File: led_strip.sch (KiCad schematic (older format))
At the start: 4 parts

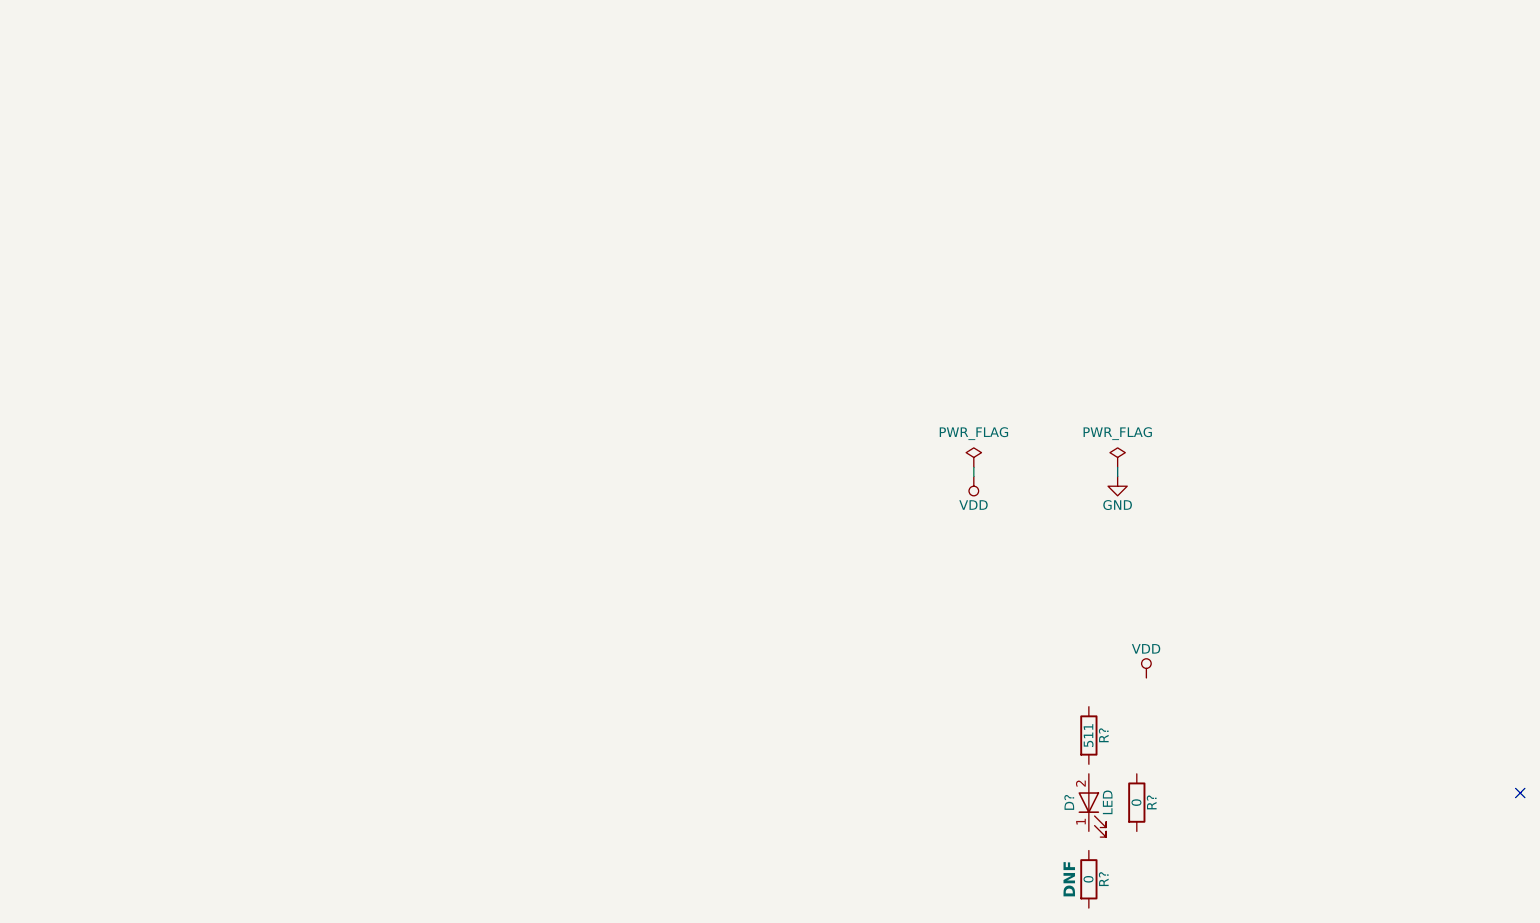
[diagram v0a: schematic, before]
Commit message: First two pages created for a hierarchical schematic. Using this as a test run to scale for the entire design
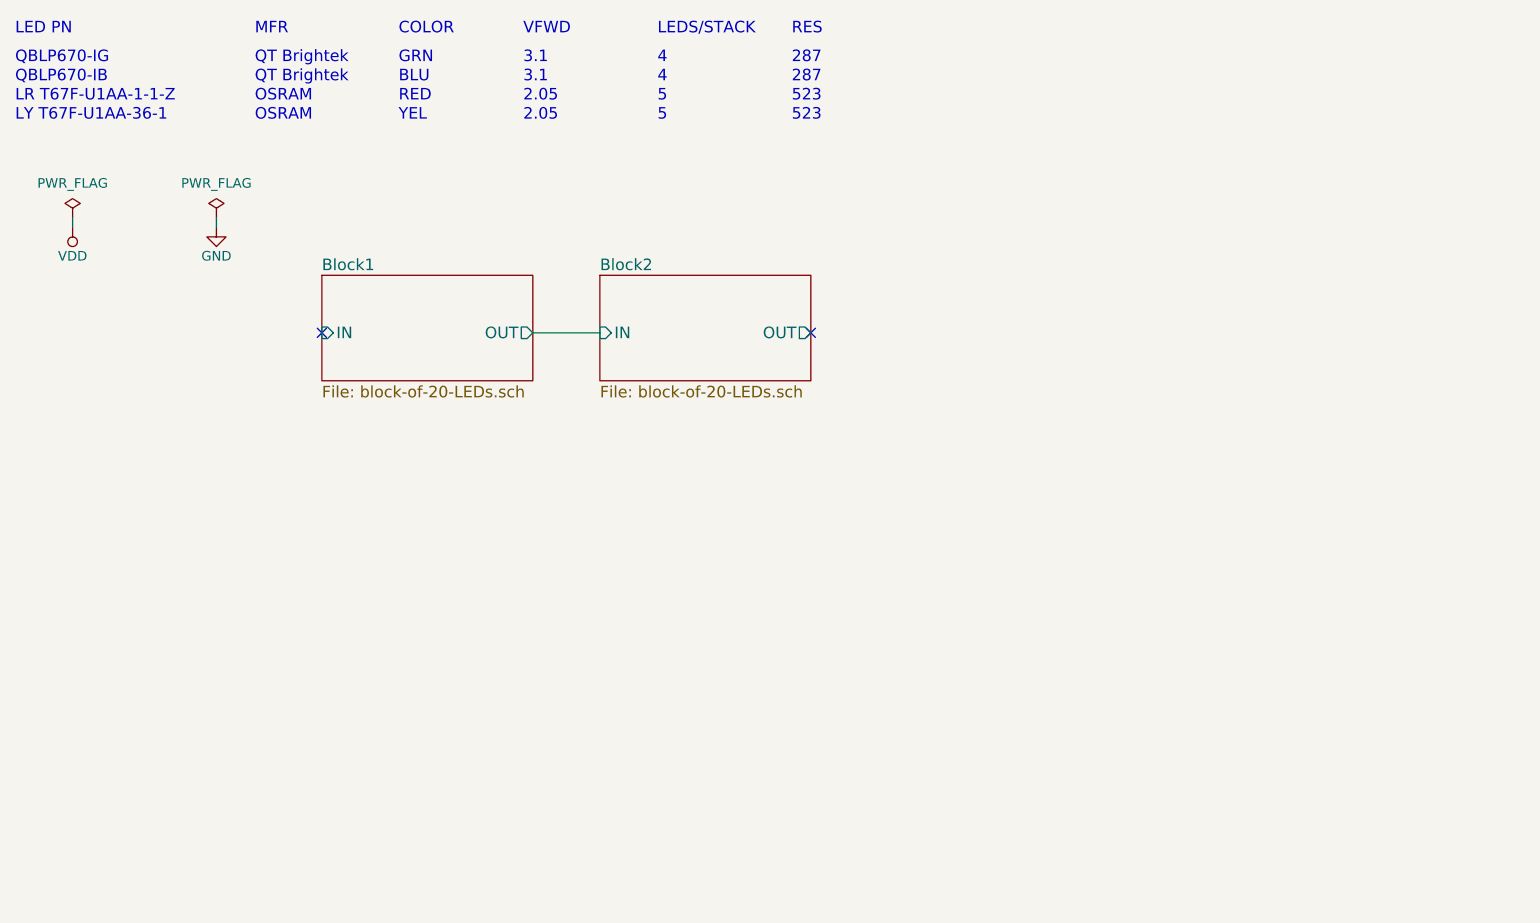
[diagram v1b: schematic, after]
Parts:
- removed D?: LED, symbol LED
- removed R?: 511, symbol R
- removed R? (x2): 0, symbol R
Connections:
- no-connect marks 1 -> 2
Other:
- note added: "2.05"
- note added: "287"
- note added: "3.1"
- note added: "4"
- note added: "5"
- note added: "523"
- note added: "BLU"
- note added: "COLOR"
- note added: "GRN"
- note added: "LED PN"
- note added: "LEDS/STACK"
- note added: "LR T67F-U1AA-1-1-Z"
- note added: "LY T67F-U1AA-36-1"
- note added: "MFR"
- note added: "OSRAM"
- note added: "QBLP670-IB"
- note added: "QBLP670-IG"
- note added: "QT Brightek"
- note added: "RED"
- note added: "RES"
- note added: "VFWD"
- note added: "YEL"
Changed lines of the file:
@@
 $Descr B 17000 11000
 encoding utf-8
-Sheet 1 1
+Sheet 1 3
 Title "LED Blade"
 Date ""
@@
 Comment4 ""
 $EndDescr
-Wire Wire Line
-	6550 3150 6550 3200
-Wire Wire Line
-	5800 3150 5800 3200
 $Comp
-L PWR_FLAG #FLG06
+L PWR_FLAG #FLG01
 U 1 1 59A4D1E2
-P 6550 3150
-F 0 "#FLG06" H 6550 3245 50  0001 C CNN
-F 1 "PWR_FLAG" H 6550 3330 50  0000 C CNN
-F 2 "" H 6550 3150 50  0000 C CNN
-F 3 "" H 6550 3150 50  0000 C CNN
-	1    6550 3150
+P 1850 1850
+F 0 "#FLG01" H 1850 1945 50  0001 C CNN
+F 1 "PWR_FLAG" H 1850 2030 50  0000 C CNN
+F 2 "" H 1850 1850 50  0000 C CNN
+F 3 "" H 1850 1850 50  0000 C CNN
+	1    1850 1850
 	1    0    0    -1
 $EndComp
 $Comp
-L GND #PWR07
+L GND #PWR02
 U 1 1 59A4D1E3
-P 6550 3200
-F 0 "#PWR07" H 6550 2950 50  0001 C CNN
-F 1 "GND" H 6550 3050 50  0000 C CNN
-F 2 "" H 6550 3200 50  0000 C CNN
-F 3 "" H 6550 3200 50  0000 C CNN
-	1    6550 3200
+P 1850 1900
+F 0 "#PWR02" H 1850 1650 50  0001 C CNN
+F 1 "GND" H 1850 1750 50  0000 C CNN
+F 2 "" H 1850 1900 50  0000 C CNN
+F 3 "" H 1850 1900 50  0000 C CNN
+	1    1850 1900
 	1    0    0    -1
 $EndComp
 $Comp
-L VDD #PWR08
+L VDD #PWR03
 U 1 1 59A4D1E4
-P 5800 3200
-F 0 "#PWR08" H 5800 3050 50  0001 C CNN
-F 1 "VDD" H 5800 3350 50  0000 C CNN
-F 2 "" H 5800 3200 50  0000 C CNN
-F 3 "" H 5800 3200 50  0000 C CNN
-	1    5800 3200
+P 1100 1900
+F 0 "#PWR03" H 1100 1750 50  0001 C CNN
+F 1 "VDD" H 1100 2050 50  0000 C CNN
+F 2 "" H 1100 1900 50  0000 C CNN
+F 3 "" H 1100 1900 50  0000 C CNN
+	1    1100 1900
 	-1   0    0    1
 $EndComp
 $Comp
-L PWR_FLAG #FLG09
+L PWR_FLAG #FLG04
 U 1 1 59A4D1E5
-P 5800 3150
-F 0 "#FLG09" H 5800 3245 50  0001 C CNN
-F 1 "PWR_FLAG" H 5800 3330 50  0000 C CNN
-F 2 "" H 5800 3150 50  0000 C CNN
-F 3 "" H 5800 3150 50  0000 C CNN
-	1    5800 3150
+P 1100 1850
+F 0 "#FLG04" H 1100 1945 50  0001 C CNN
+F 1 "PWR_FLAG" H 1100 2030 50  0000 C CNN
+F 2 "" H 1100 1850 50  0000 C CNN
+F 3 "" H 1100 1850 50  0000 C CNN
+	1    1100 1850
 	1    0    0    -1
 $EndComp
-NoConn ~ 8650 4850
-$Comp
-L R R?
-U 1 1 59AADD53
-P 6400 4550
-F 0 "R?" V 6480 4550 50  0000 C CNN
-F 1 "511" V 6400 4550 50  0000 C CNN
-F 2 "" V 6330 4550 50  0001 C CNN
-F 3 "" H 6400 4550 50  0001 C CNN
-F 4 "~" H 6400 4550 60  0001 C CNN "Manufacturer"
-F 5 "~" H 6400 4550 60  0001 C CNN "Manufacturer Part Number"
-F 6 "0805" H 6400 4550 60  0001 C CNN "Package"
-F 7 "RES, 0805, 511, 1%" H 6400 4550 60  0001 C CNN "Description"
-F 8 "True" H 6400 4550 60  0001 C CNN "Fitted"
-F 9 "~" H 6400 4550 60  0001 C CNN "Notes"
-	1    6400 4550
-	1    0    0    -1
-$EndComp
-$Comp
-L LED D?
-U 1 1 59AADFAA
-P 6400 4900
-F 0 "D?" H 6400 5000 50  0000 C CNN
-F 1 "LED" H 6400 4800 50  0000 C CNN
-F 2 "" H 6400 4900 50  0001 C CNN
-F 3 "" H 6400 4900 50  0001 C CNN
-	1    6400 4900
-	0    -1   -1   0
-$EndComp
-$Comp
-L R R?
-U 1 1 59AAE06F
-P 6650 4900
-F 0 "R?" V 6730 4900 50  0000 C CNN
-F 1 "0" V 6650 4900 50  0000 C CNN
-F 2 "" V 6580 4900 50  0001 C CNN
-F 3 "" H 6650 4900 50  0001 C CNN
-F 4 "~" H 6650 4900 60  0001 C CNN "Manufacturer"
-F 5 "~" H 6650 4900 60  0001 C CNN "Manufacturer Part Number"
-F 6 "0805" H 6650 4900 60  0001 C CNN "Package"
-F 7 "RES, 0805, JUMPER" H 6650 4900 60  0001 C CNN "Description"
-F 8 "True" H 6650 4900 60  0001 C CNN "Fitted"
-F 9 "~" H 6650 4900 60  0001 C CNN "Notes"
-	1    6650 4900
-	1    0    0    -1
-$EndComp
-$Comp
-L VDD #PWR?
-U 1 1 59AAE2E6
-P 6700 4250
-F 0 "#PWR?" H 6700 4100 50  0001 C CNN
-F 1 "VDD" H 6700 4400 50  0000 C CNN
-F 2 "" H 6700 4250 50  0000 C CNN
-F 3 "" H 6700 4250 50  0000 C CNN
-	1    6700 4250
-	1    0    0    -1
-$EndComp
-$Comp
-L R R?
-U 1 1 59AAE340
-P 6400 5300
-F 0 "R?" V 6480 5300 50  0000 C CNN
-F 1 "0" V 6400 5300 50  0000 C CNN
-F 2 "" V 6330 5300 50  0001 C CNN
-F 3 "" H 6400 5300 50  0001 C CNN
-F 4 "~" H 6400 5300 60  0001 C CNN "Manufacturer"
-F 5 "~" H 6400 5300 60  0001 C CNN "Manufacturer Part Number"
-F 6 "0805" H 6400 5300 60  0001 C CNN "Package"
-F 7 "RES, 0805, JUMPER" H 6400 5300 60  0001 C CNN "Description"
-F 8 "DNF" V 6300 5300 60  0000 C CNB "Fitted"
-F 9 "~" H 6400 5300 60  0001 C CNN "Notes"
-	1    6400 5300
-	1    0    0    -1
-$EndComp
+Text Notes 800  1050 0    60   ~ 0
+QBLP670-IG
+Text Notes 800  900  0    60   ~ 0
+LED PN
+Text Notes 2050 900  0    60   ~ 0
+MFR
+Text Notes 2800 900  0    60   ~ 0
+COLOR
+Text Notes 4150 900  0    60   ~ 0
+LEDS/STACK
+Text Notes 4850 900  0    60   ~ 0
+RES
+Text Notes 3450 900  0    60   ~ 0
+VFWD
+Text Notes 2050 1050 0    60   ~ 0
+QT Brightek
+Text Notes 2800 1050 0    60   ~ 0
+GRN
+Text Notes 3450 1050 0    60   ~ 0
+3.1
+Text Notes 4150 1050 0    60   ~ 0
+4
+Text Notes 4850 1050 0    60   ~ 0
+287
+Text Notes 800  1150 0    60   ~ 0
+QBLP670-IB
+Text Notes 2050 1150 0    60   ~ 0
+QT Brightek
+Text Notes 2800 1150 0    60   ~ 0
+BLU
+Text Notes 3450 1150 0    60   ~ 0
+3.1
+Text Notes 4150 1150 0    60   ~ 0
+4
+Text Notes 4850 1150 0    60   ~ 0
+287
+Text Notes 800  1250 0    60   ~ 0
+LR T67F-U1AA-1-1-Z
+Text Notes 2050 1250 0    60   ~ 0
+OSRAM
+Text Notes 2800 1250 0    60   ~ 0
+RED
+Text Notes 3450 1250 0    60   ~ 0
+2.05
+Text Notes 4150 1250 0    60   ~ 0
+5
+Text Notes 4850 1250 0    60   ~ 0
+523
+Text Notes 800  1350 0    60   ~ 0
+LY T67F-U1AA-36-1
+Text Notes 2050 1350 0    60   ~ 0
+OSRAM
+Text Notes 2800 1350 0    60   ~ 0
+YEL
+Text Notes 3450 1350 0    60   ~ 0
+2.05
+Text Notes 4150 1350 0    60   ~ 0
+5
+Text Notes 4850 1350 0    60   ~ 0
+523
+Wire Wire Line
+	1850 1850 1850 1900
+Wire Wire Line
+	1100 1850 1100 1900
+$Sheet
+S 2400 2150 1100 550
+U 59AB9263
+F0 "Block1" 60
+F1 "block-of-20-LEDs.sch" 60
+F2 "IN" I L 2400 2450 60
+F3 "OUT" O R 3500 2450 60
+$EndSheet
+$Sheet
+S 3850 2150 1100 550
+U 59AB246C
+F0 "Block2" 60
+F1 "block-of-20-LEDs.sch" 60
+F2 "IN" I L 3850 2450 60
+F3 "OUT" O R 4950 2450 60
+$EndSheet
+NoConn ~ 2400 2450
+NoConn ~ 4950 2450
+Wire Wire Line
+	3500 2450 3850 2450
 $EndSCHEMATC

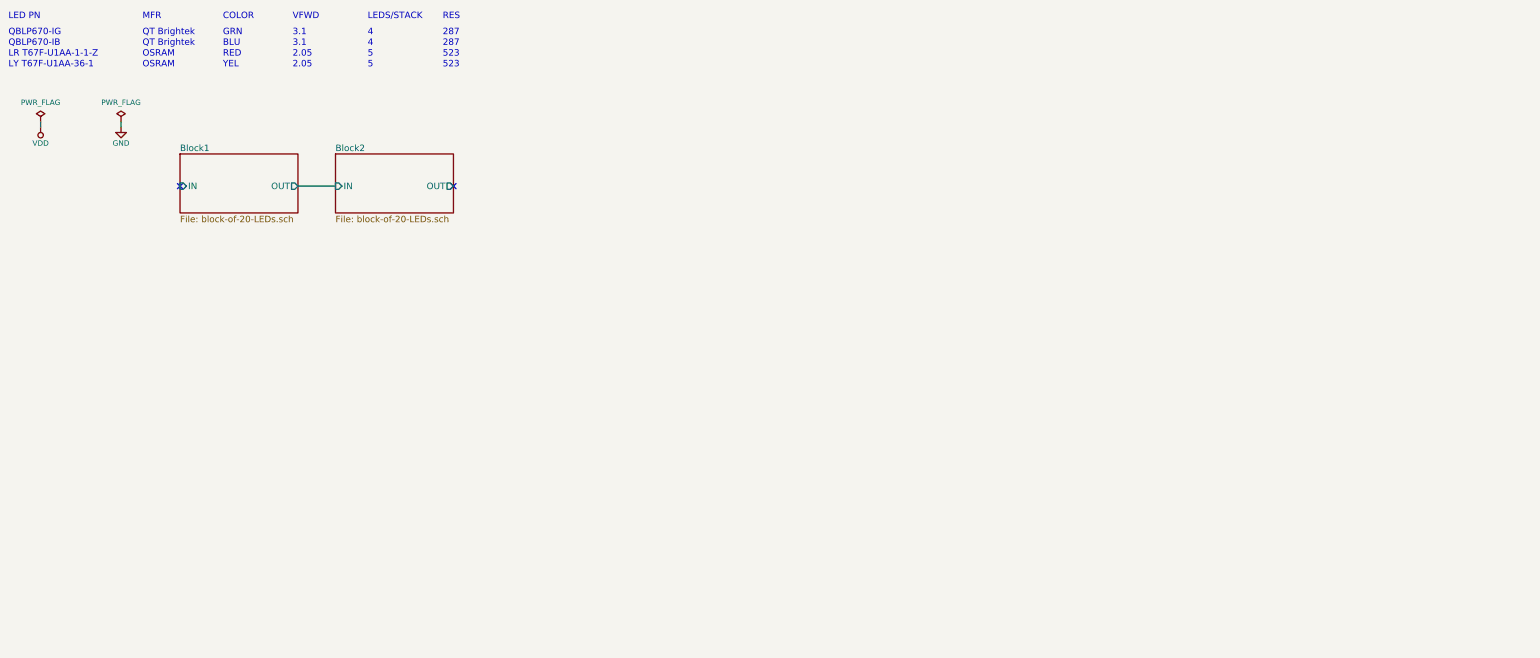
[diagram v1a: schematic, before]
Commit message: Schematic and layout complete. Just need to work on getting the BOM in a good format
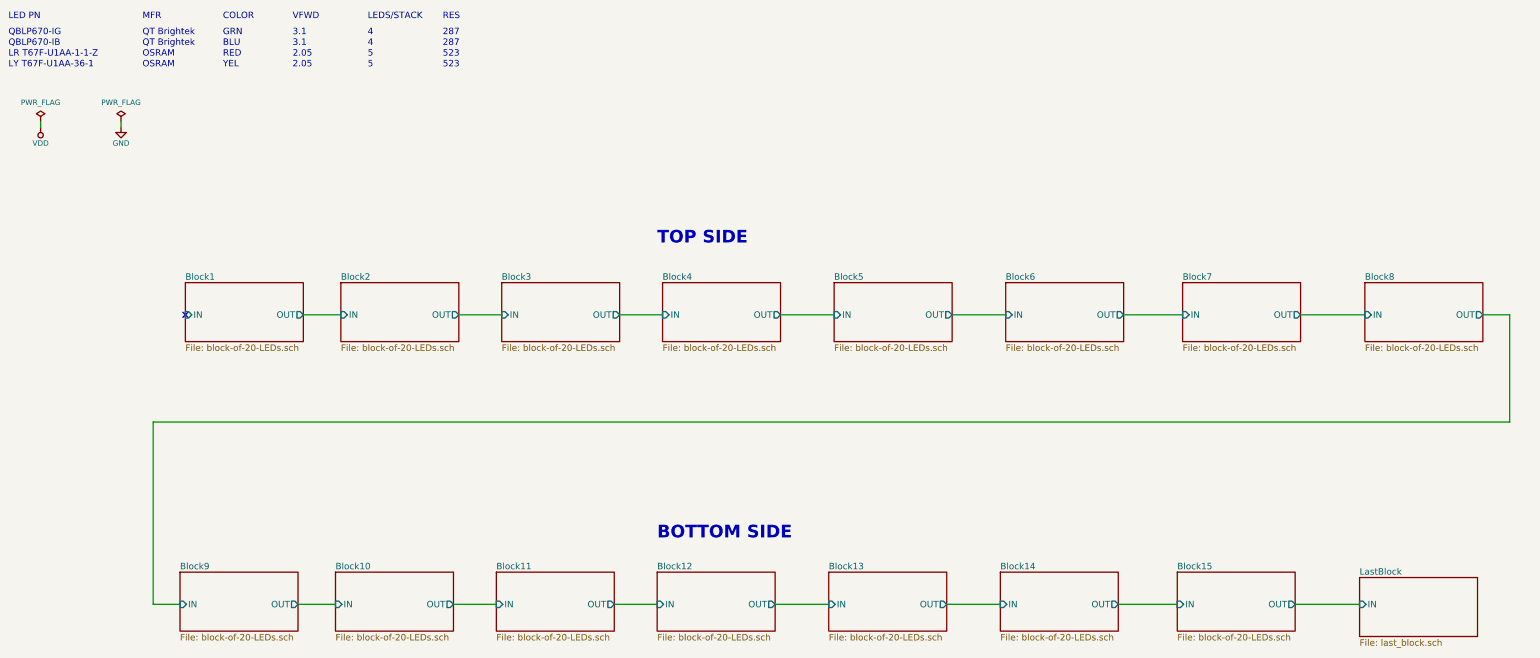
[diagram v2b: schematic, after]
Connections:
- no-connect marks 2 -> 1
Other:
- note added: "BOTTOM SIDE"
- note added: "TOP SIDE"
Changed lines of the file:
@@
 $Descr B 17000 11000
 encoding utf-8
-Sheet 1 3
-Title "LED Blade"
+Sheet 1 17
+Title "SBR001-201"
 Date ""
-Rev "X1"
-Comp ""
+Rev "A"
+Comp "Saber Forge"
 Comment1 ""
 Comment2 ""
@@
 	1100 1850 1100 1900
 $Sheet
-S 2400 2150 1100 550
+S 2450 3350 1100 550
 U 59AB9263
 F0 "Block1" 60
 F1 "block-of-20-LEDs.sch" 60
-F2 "IN" I L 2400 2450 60
-F3 "OUT" O R 3500 2450 60
-$EndSheet
-$Sheet
-S 3850 2150 1100 550
+F2 "IN" I L 2450 3650 60
+F3 "OUT" O R 3550 3650 60
+$EndSheet
+$Sheet
+S 3900 3350 1100 550
 U 59AB246C
 F0 "Block2" 60
 F1 "block-of-20-LEDs.sch" 60
-F2 "IN" I L 3850 2450 60
-F3 "OUT" O R 4950 2450 60
-$EndSheet
-NoConn ~ 2400 2450
-NoConn ~ 4950 2450
-Wire Wire Line
-	3500 2450 3850 2450
+F2 "IN" I L 3900 3650 60
+F3 "OUT" O R 5000 3650 60
+$EndSheet
+NoConn ~ 2450 3650
+Wire Wire Line
+	3550 3650 3900 3650
+$Sheet
+S 5400 3350 1100 550
+U 59AC6B82
+F0 "Block3" 60
+F1 "block-of-20-LEDs.sch" 60
+F2 "IN" I L 5400 3650 60
+F3 "OUT" O R 6500 3650 60
+$EndSheet
+$Sheet
+S 6900 3350 1100 550
+U 59AC6E57
+F0 "Block4" 60
+F1 "block-of-20-LEDs.sch" 60
+F2 "IN" I L 6900 3650 60
+F3 "OUT" O R 8000 3650 60
+$EndSheet
+$Sheet
+S 8500 3350 1100 550
+U 59AC6FF9
+F0 "Block5" 60
+F1 "block-of-20-LEDs.sch" 60
+F2 "IN" I L 8500 3650 60
+F3 "OUT" O R 9600 3650 60
+$EndSheet
+$Sheet
+S 10100 3350 1100 550
+U 59AC7105
+F0 "Block6" 60
+F1 "block-of-20-LEDs.sch" 60
+F2 "IN" I L 10100 3650 60
+F3 "OUT" O R 11200 3650 60
+$EndSheet
+$Sheet
+S 11750 3350 1100 550
+U 59AC71E1
+F0 "Block7" 60
+F1 "block-of-20-LEDs.sch" 60
+F2 "IN" I L 11750 3650 60
+F3 "OUT" O R 12850 3650 60
+$EndSheet
+$Sheet
+S 13450 3350 1100 550
+U 59AC74FD
+F0 "Block8" 60
+F1 "block-of-20-LEDs.sch" 60
+F2 "IN" I L 13450 3650 60
+F3 "OUT" O R 14550 3650 60
+$EndSheet
+Wire Wire Line
+	5000 3650 5400 3650
+Wire Wire Line
+	6500 3650 6900 3650
+Wire Wire Line
+	8000 3650 8500 3650
+Wire Wire Line
+	9600 3650 10100 3650
+Wire Wire Line
+	11200 3650 11750 3650
+Wire Wire Line
+	12850 3650 13450 3650
+Text Notes 6850 3000 0    118  ~ 24
+TOP SIDE
+Text Notes 6850 5750 0    118  ~ 24
+BOTTOM SIDE
+$Sheet
+S 2400 6050 1100 550
+U 59AC8D70
+F0 "Block9" 60
+F1 "block-of-20-LEDs.sch" 60
+F2 "IN" I L 2400 6350 60
+F3 "OUT" O R 3500 6350 60
+$EndSheet
+$Sheet
+S 3850 6050 1100 550
+U 59AC8D74
+F0 "Block10" 60
+F1 "block-of-20-LEDs.sch" 60
+F2 "IN" I L 3850 6350 60
+F3 "OUT" O R 4950 6350 60
+$EndSheet
+Wire Wire Line
+	3500 6350 3850 6350
+$Sheet
+S 5350 6050 1100 550
+U 59AC8D7A
+F0 "Block11" 60
+F1 "block-of-20-LEDs.sch" 60
+F2 "IN" I L 5350 6350 60
+F3 "OUT" O R 6450 6350 60
+$EndSheet
+$Sheet
+S 6850 6050 1100 550
+U 59AC8D7E
+F0 "Block12" 60
+F1 "block-of-20-LEDs.sch" 60
+F2 "IN" I L 6850 6350 60
+F3 "OUT" O R 7950 6350 60
+$EndSheet
+$Sheet
+S 8450 6050 1100 550
+U 59AC8D82
+F0 "Block13" 60
+F1 "block-of-20-LEDs.sch" 60
+F2 "IN" I L 8450 6350 60
+F3 "OUT" O R 9550 6350 60
+$EndSheet
+$Sheet
+S 10050 6050 1100 550
+U 59AC8D86
+F0 "Block14" 60
+F1 "block-of-20-LEDs.sch" 60
+F2 "IN" I L 10050 6350 60
+F3 "OUT" O R 11150 6350 60
+$EndSheet
+$Sheet
+S 11700 6050 1100 550
+U 59AC8D8A
+F0 "Block15" 60
+F1 "block-of-20-LEDs.sch" 60
+F2 "IN" I L 11700 6350 60
+F3 "OUT" O R 12800 6350 60
+$EndSheet
+Wire Wire Line
+	4950 6350 5350 6350
+Wire Wire Line
+	6450 6350 6850 6350
+Wire Wire Line
+	7950 6350 8450 6350
+Wire Wire Line
+	9550 6350 10050 6350
+Wire Wire Line
+	11150 6350 11700 6350
+Wire Wire Line
+	12800 6350 13400 6350
+$Sheet
+S 13400 6100 1100 550
+U 59ACC944
+F0 "LastBlock" 60
+F1 "last_block.sch" 60
+F2 "IN" I L 13400 6350 60
+$EndSheet
+Wire Wire Line
+	14550 3650 14800 3650
+Wire Wire Line
+	14800 3650 14800 4650
+Wire Wire Line
+	14800 4650 2150 4650
+Wire Wire Line
+	2150 4650 2150 6350
+Wire Wire Line
+	2150 6350 2400 6350
 $EndSCHEMATC
